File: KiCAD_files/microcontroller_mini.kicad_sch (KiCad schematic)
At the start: 35 parts, among them J1 Conn_02x20_Top_Bottom, J2 USB_C_Receptacle_USB2.0, J8 FTSH-107-01-F-DV-K, SW1 KMR241NGLFS, SW2 KMR241NGLFS, U1 STM32G474RE, U3 WE-TVS-82400102, U4 AP1117-33, Y1 ECS-240-10-33-AGM-TR - 24MHz

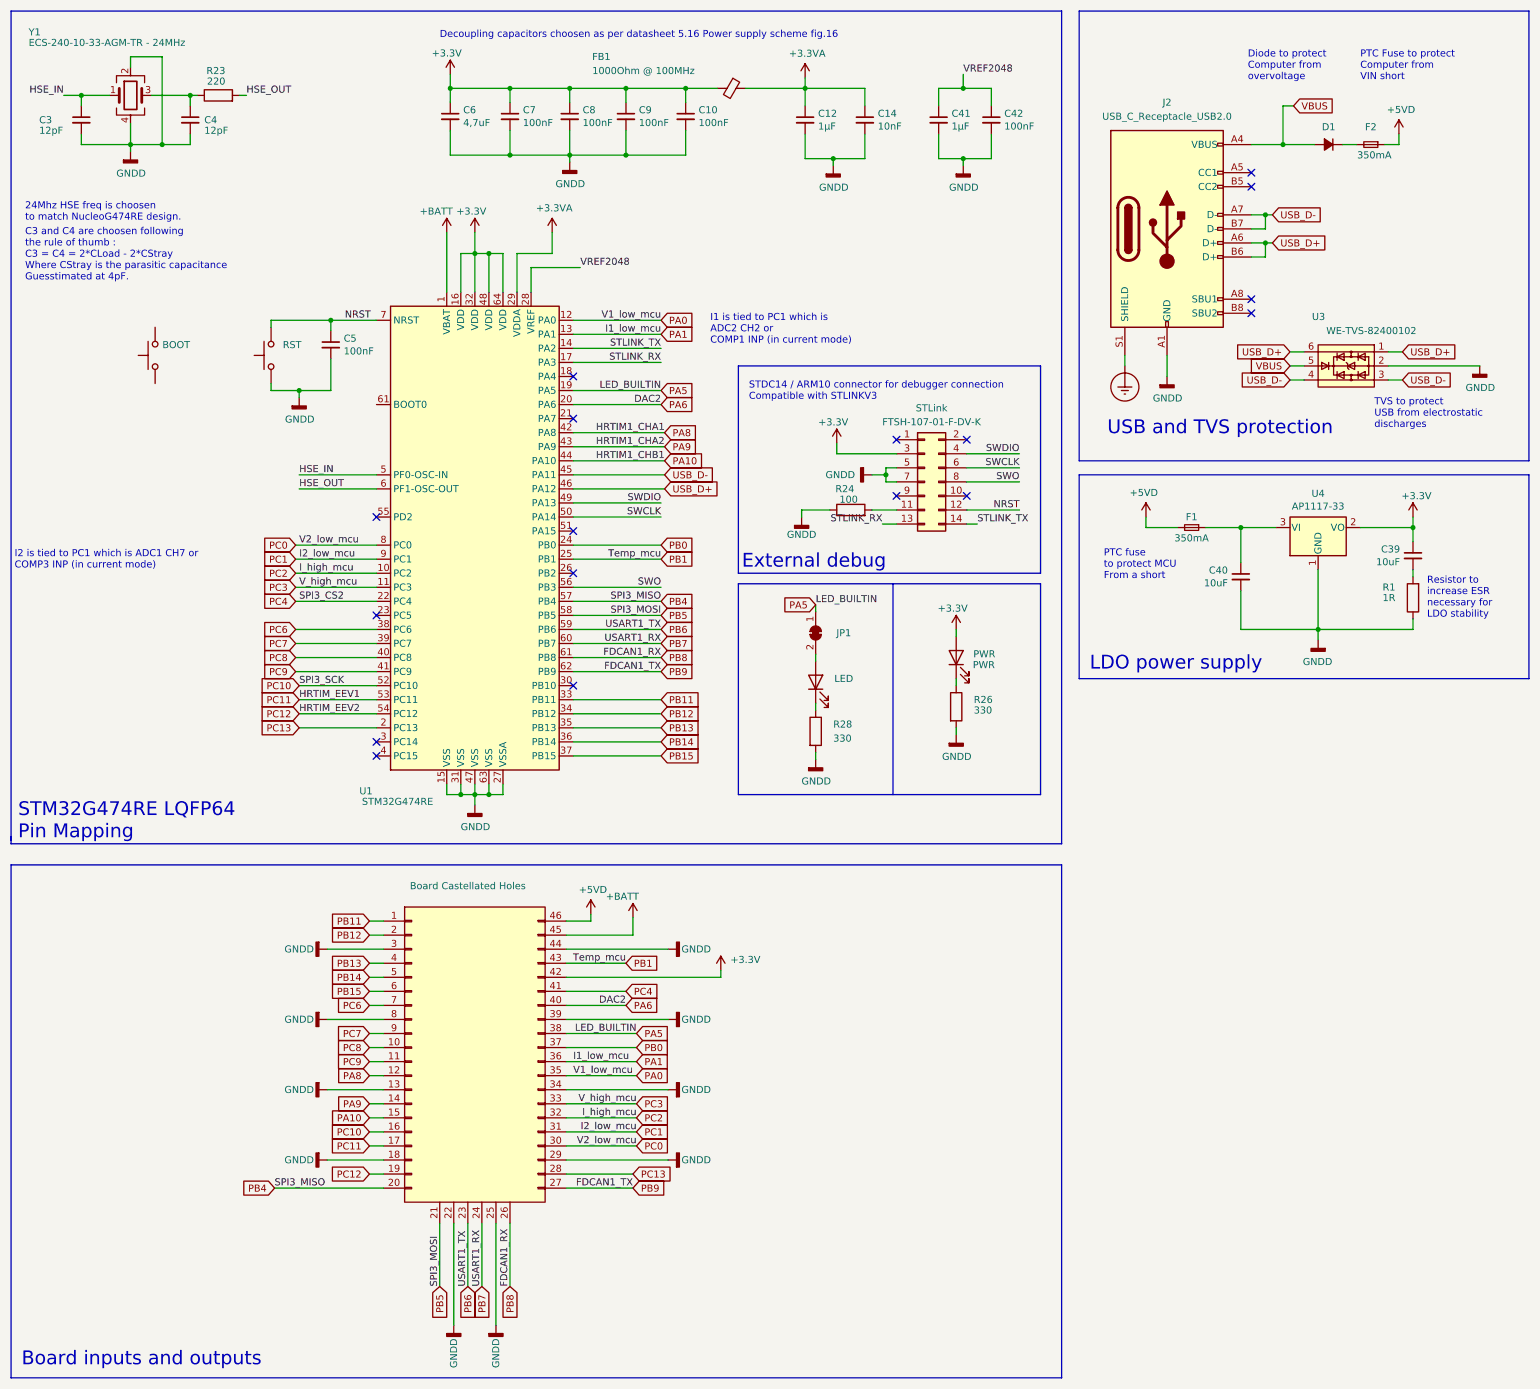
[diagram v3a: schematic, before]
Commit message: WIP : Finalized the rework of the MCU board. Added extra pins to be able to interact with all the native pinout of the G474 Choosen to deploy the bootloader pin on PC14, it will require a custom bootloader.
Former-commit-id: c1ded6b4e2272d08c1bdd5e172bcf8412ac79a26
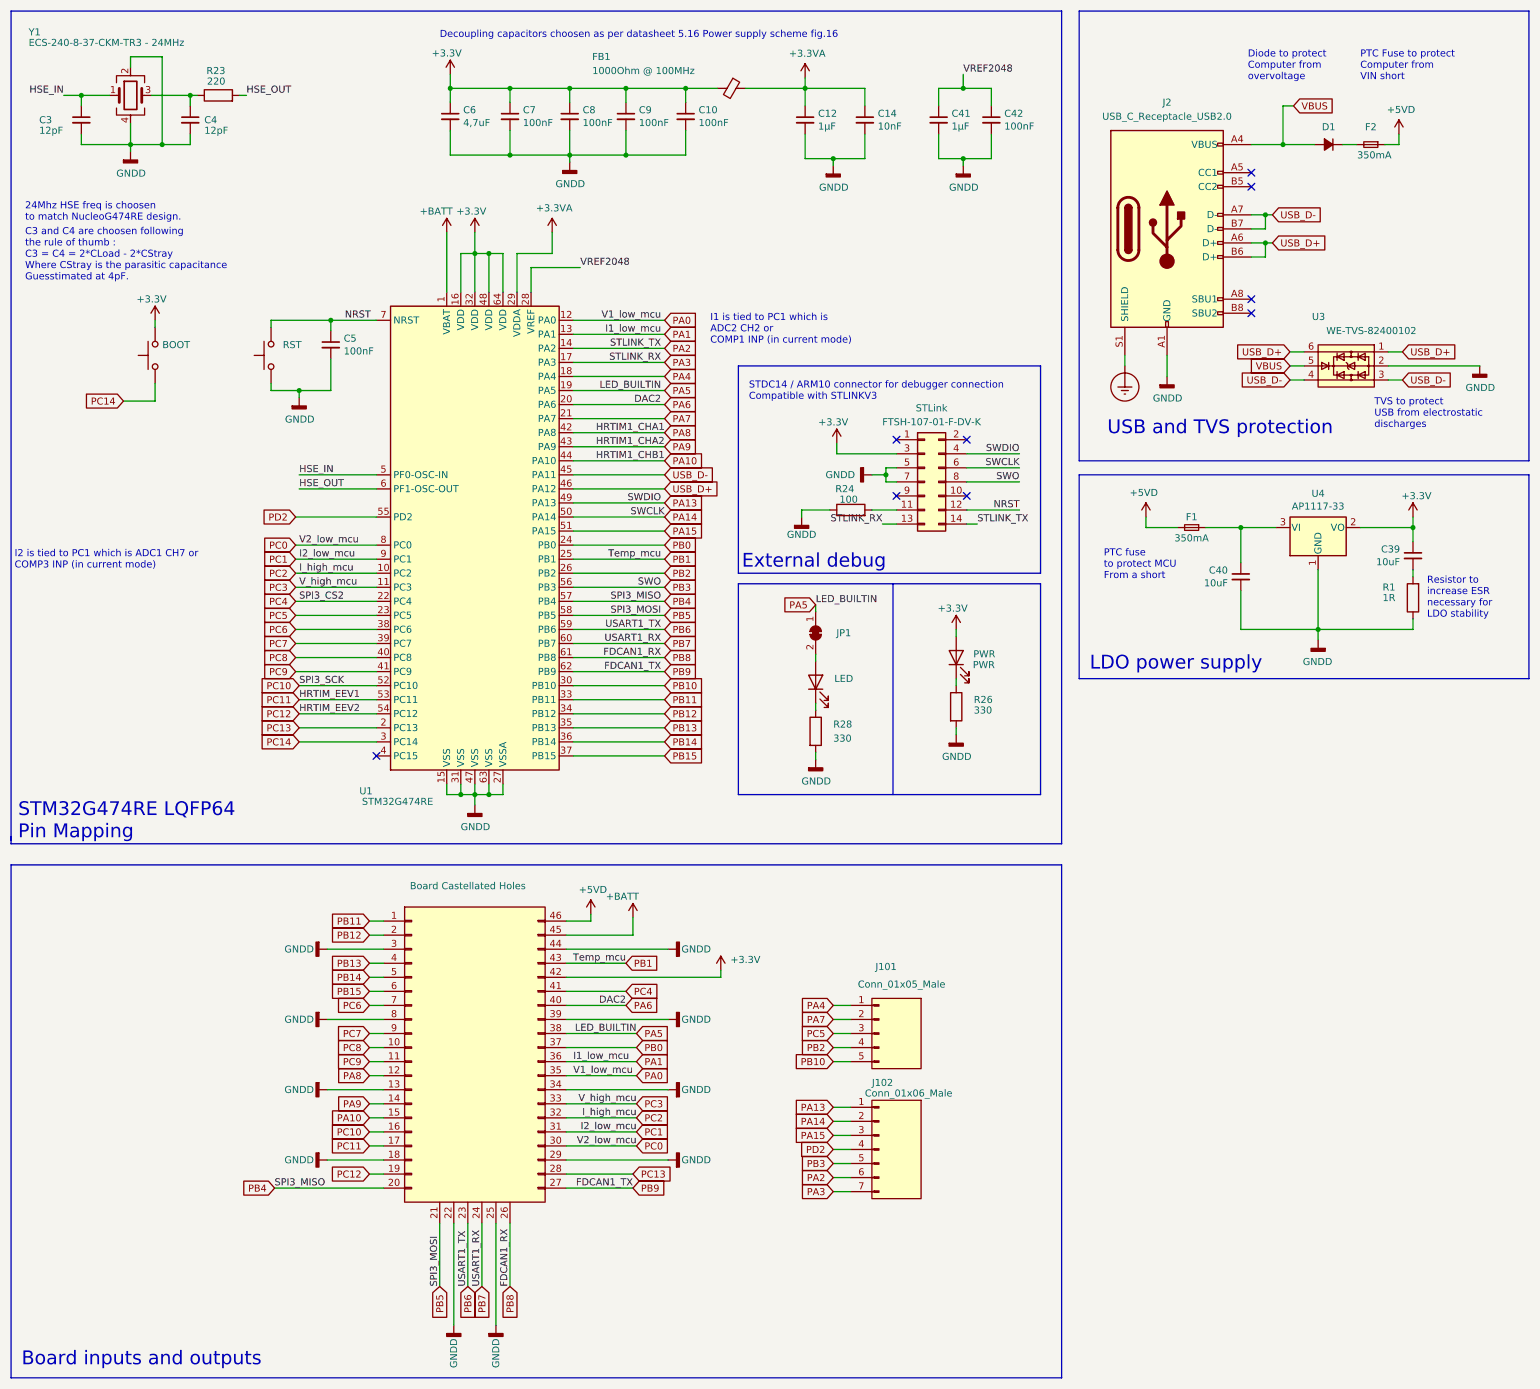
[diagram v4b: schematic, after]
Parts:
- added J101: Conn_01x05_Male, Footprints:PinHeader_1x05_P2.54mm_Vertical, symbol Connector:Conn_01x05_Male
- added J102: Conn_01x06_Male, Footprints:PinHeader_1x07_P2.54mm_Vertical, symbol Connector:Conn_01x07_Male
- Y1: value ECS-240-10-33-AGM-TR - 24MHz -> ECS-240-8-37-CKM-TR3 - 24MHz; footprint Crystal:Crystal_SMD_3225-4Pin_3.2x2.5mm -> Crystal:Crystal_SMD_2016-4Pin_2.0x1.6mm; Manf# ECS-240-10-33-AGM-TR -> ECS-240-8-37-CKM-TR3
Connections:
- net +3V3: now also SW2.2
- net PA4: now reaches U1.18 (PA4)
- net PA4: now also J101.1 (Pin_1)
- net PA7: now reaches U1.21 (PA7)
- net PA7: now also J101.2 (Pin_2)
- net PC5: now reaches U1.23 (PC5)
- net PC5: now also J101.3 (Pin_3)
- net PB2: now reaches U1.26 (PB2)
- net PB2: now also J101.4 (Pin_4)
- net PC14: now reaches U1.3 (PC14)
- net PC14: now also SW2.1
- net PB10: now reaches U1.30 (PB10)
- net PB10: now also J101.5 (Pin_5)
- net PA15: now reaches U1.51 (PA15)
- net PA15: now also J102.3 (Pin_3)
- net PD2: now reaches U1.55 (PD2)
- net PD2: now also J102.4 (Pin_4)
- net STLINK_RX renamed PA3
- net PA3: now also J102.7 (Pin_7)
- net STLINK_TX renamed PA2
- net PA2: now also J102.6 (Pin_6)
- net SWCLK renamed PA14
- net PA14: now also J102.2 (Pin_2)
- net SWDIO renamed PA13
- net PA13: now also J102.1 (Pin_1)
- net SWO renamed PB3
- net PB3: now also J102.5 (Pin_5)
- no-connect marks 17 -> 9

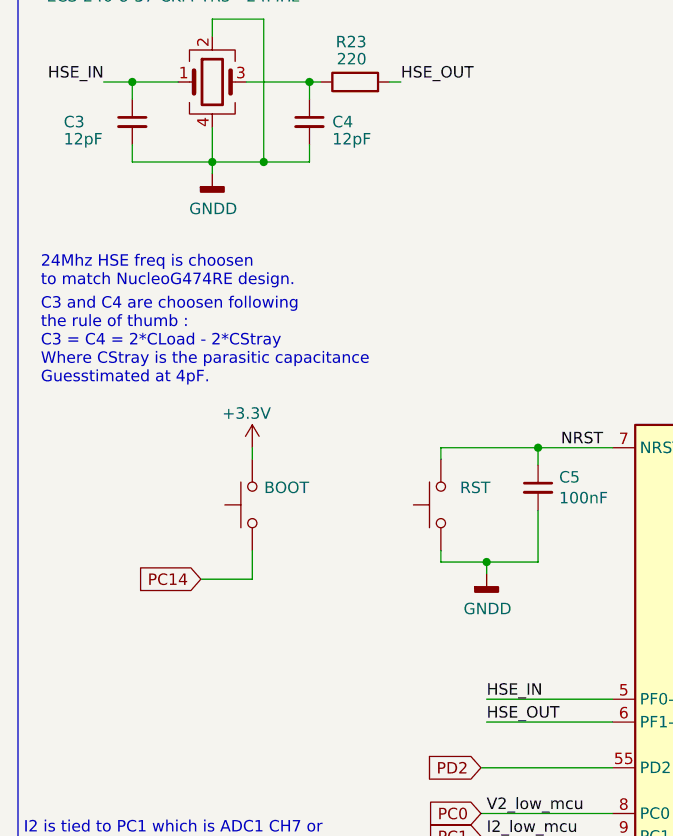
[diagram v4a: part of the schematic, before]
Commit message: WIP : Refined the crystal GND keepout, polished the bottom overlay
Former-commit-id: 2906c1a23d44a8ddcb814e6c8993671dfbd082db
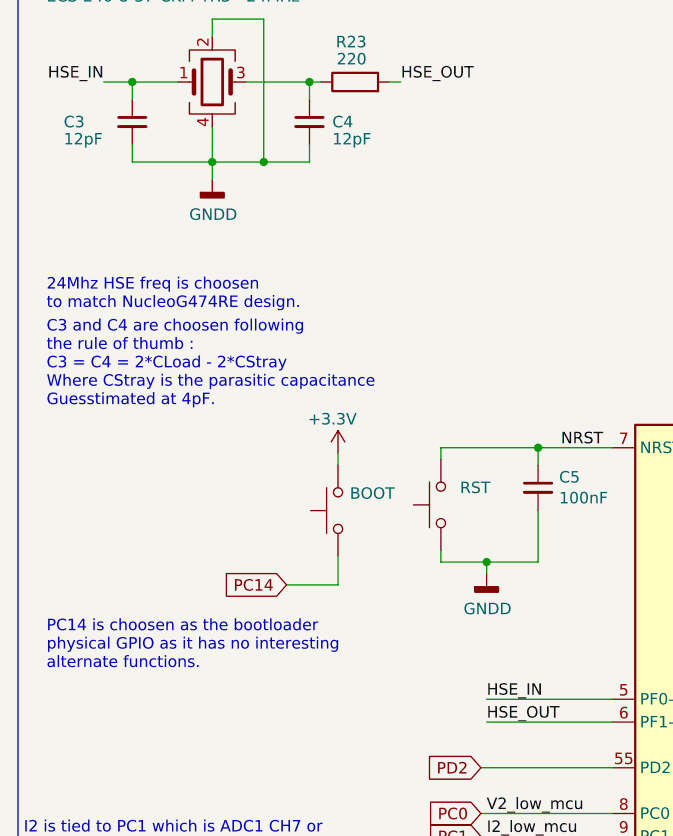
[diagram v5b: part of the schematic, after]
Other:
- note added: "PC14 is choosen as the bootloader physical GPIO as it has no interesting alternate functions."
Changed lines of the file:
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@@
   (no_connect (at 177.8 100.33))
   (no_connect (at 83.82 157.48))
-  (wire (pts (xy 43.815 78.74) (xy 43.815 80.01))
+  (wire (pts (xy 53.34 79.375) (xy 53.34 80.645))
     (stroke (width 0) (type default) (color 0 0 0 0))
   )
@@
     (stroke (width 0) (type default) (color 0 0 0 0))
   )
-  (wire (pts (xy 39.37 46.99) (xy 39.37 48.26))
-    (stroke (width 0) (type default) (color 0 0 0 0))
-  )
   (polyline (pts (xy 207.645 177.165) (xy 17.78 177.165))
     (stroke (width 0) (type default) (color 0 0 0 0))
@@
     (stroke (width 0) (type default) (color 0 0 0 0))
   )
-  (wire (pts (xy 43.815 90.17) (xy 43.815 93.345))
+  (wire (pts (xy 53.34 90.805) (xy 53.34 93.98))
     (stroke (width 0) (type default) (color 0 0 0 0))
   )
@@
     (stroke (width 0) (type default) (color 0 0 0 0))
   )
-  (wire (pts (xy 38.1 93.345) (xy 43.815 93.345))
+  (wire (pts (xy 47.625 93.98) (xy 53.34 93.98))
     (stroke (width 0) (type default) (color 0 0 0 0))
   )
@@
     (stroke (width 0) (type default) (color 0 0 0 0))
   )
+  (wire (pts (xy 39.37 46.99) (xy 39.37 48.895))
+    (stroke (width 0) (type default) (color 0 0 0 0))
+  )
   (wire (pts (xy 119.38 91.44) (xy 135.89 91.44))
     (stroke (width 0) (type default) (color 0 0 0 0))
@@
   (wire (pts (xy 172.085 40.005) (xy 172.085 36.83))
     (stroke (width 0) (type default) (color 0 0 0 0))
+  )
+  (text "PC14 is choosen as the bootloader \nphysical GPIO as it has no interesting\nalternate functions."
+    (at 20.955 103.505 0)
+    (effects (font (size 1.27 1.27)) (justify left bottom))
   )
   (text "PTC Fuse to protect \nComputer from \nVIN short" (at 261.62 35.56 0)
@@
   )
   (text "C3 and C4 are choosen following \nthe rule of thumb : \nC3 = C4 = 2*CLoad - 2*CStray \nWhere CStray is the parasitic capacitance\nGuesstimated at 4pF."
-    (at 20.32 71.755 0)
+    (at 20.955 74.295 0)
     (effects (font (size 1.27 1.27)) (justify left bottom))
   )
@@
   )
   (text "24Mhz HSE freq is choosen\nto match NucleoG474RE design. "
-    (at 20.32 60.96 0)
+    (at 20.955 63.5 0)
     (effects (font (size 1.27 1.27)) (justify left bottom))
   )
@@
     )
   )
-  (global_label "PC14" (shape input) (at 38.1 93.345 180) (fields_autoplaced)
-    (effects (font (size 1.27 1.27)) (justify right))
-    (property "Références Inter-Feuilles" "${INTERSHEET_REFS}" (id 0) (at 30.7279 93.2656 0)
+  (global_label "PC14" (shape input) (at 47.625 93.98 180) (fields_autoplaced)
+    (effects (font (size 1.27 1.27)) (justify right))
+    (property "Références Inter-Feuilles" "${INTERSHEET_REFS}" (id 0) (at 40.2529 93.9006 0)
       (effects (font (size 1.27 1.27)) (justify right) hide)
     )
@@
     (pin "2")
   )
-  (symbol (lib_id "power:GNDD") (at 39.37 48.26 0) (unit 1)
-    (in_bom yes) (on_board yes)
-    (property "Reference" "#PWR01" (id 0) (at 39.37 54.61 0)
-      (effects (font (size 1.27 1.27)) hide)
-    )
-    (property "Value" "GNDD" (id 1) (at 39.4716 52.197 0))
-    (property "Footprint" "" (id 2) (at 39.37 48.26 0)
-      (effects (font (size 1.27 1.27)) hide)
-    )
-    (property "Datasheet" "" (id 3) (at 39.37 48.26 0)
+  (symbol (lib_id "power:GNDD") (at 39.37 48.895 0) (unit 1)
+    (in_bom yes) (on_board yes)
+    (property "Reference" "#PWR01" (id 0) (at 39.37 55.245 0)
+      (effects (font (size 1.27 1.27)) hide)
+    )
+    (property "Value" "GNDD" (id 1) (at 39.4716 52.832 0))
+    (property "Footprint" "" (id 2) (at 39.37 48.895 0)
+      (effects (font (size 1.27 1.27)) hide)
+    )
+    (property "Datasheet" "" (id 3) (at 39.37 48.895 0)
       (effects (font (size 1.27 1.27)) hide)
     )
@@
     (pin "1")
   )
-  (symbol (lib_id "Switch:SW_Push") (at 43.815 85.09 90) (unit 1)
-    (in_bom yes) (on_board yes)
-    (property "Reference" "SW2" (id 0) (at 45.0342 83.9216 90)
-      (effects (font (size 1.27 1.27)) (justify right) hide)
-    )
-    (property "Value" "KMR241NGLFS" (id 1) (at 45.0342 86.233 90)
-      (effects (font (size 1.27 1.27)) (justify right) hide)
-    )
-    (property "Footprint" "Button_Switch_SMD:SW_Push_1P1T_NO_CK_KMR2" (id 2) (at 38.735 85.09 0)
-      (effects (font (size 1.27 1.27)) hide)
-    )
-    (property "Datasheet" "~" (id 3) (at 38.735 85.09 0)
-      (effects (font (size 1.27 1.27)) hide)
-    )
-    (property "Manf#" "KMR241NGLFS" (id 4) (at 43.815 85.09 0)
-      (effects (font (size 1.27 1.27)) hide)
-    )
-    (property "Name" "BOOT" (id 5) (at 47.625 83.185 90))
+  (symbol (lib_id "Switch:SW_Push") (at 53.34 85.725 90) (unit 1)
+    (in_bom yes) (on_board yes)
+    (property "Reference" "SW2" (id 0) (at 54.5592 84.5566 90)
+      (effects (font (size 1.27 1.27)) (justify right) hide)
+    )
+    (property "Value" "KMR241NGLFS" (id 1) (at 54.5592 86.868 90)
+      (effects (font (size 1.27 1.27)) (justify right) hide)
+    )
+    (property "Footprint" "Button_Switch_SMD:SW_Push_1P1T_NO_CK_KMR2" (id 2) (at 48.26 85.725 0)
+      (effects (font (size 1.27 1.27)) hide)
+    )
+    (property "Datasheet" "~" (id 3) (at 48.26 85.725 0)
+      (effects (font (size 1.27 1.27)) hide)
+    )
+    (property "Manf#" "KMR241NGLFS" (id 4) (at 53.34 85.725 0)
+      (effects (font (size 1.27 1.27)) hide)
+    )
+    (property "Name" "BOOT" (id 5) (at 57.15 83.82 90))
     (pin "1")
     (pin "2")
@@
     (pin "1")
   )
-  (symbol (lib_id "power:+3.3V") (at 43.815 78.74 0) (unit 1)
-    (in_bom yes) (on_board yes)
-    (property "Reference" "#PWR0109" (id 0) (at 43.815 82.55 0)
-      (effects (font (size 1.27 1.27)) hide)
-    )
-    (property "Value" "+3.3V" (id 1) (at 43.18 74.93 0))
-    (property "Footprint" "" (id 2) (at 43.815 78.74 0)
-      (effects (font (size 1.27 1.27)) hide)
-    )
-    (property "Datasheet" "" (id 3) (at 43.815 78.74 0)
-      (effects (font (size 1.27 1.27)) hide)
-    )
+  (symbol (lib_id "power:+3.3V") (at 53.34 79.375 0) (unit 1)
+    (in_bom yes) (on_board yes)
+    (property "Reference" "#PWR0109" (id 0) (at 53.34 83.185 0)
+      (effects (font (size 1.27 1.27)) hide)
+    )
+    (property "Value" "+3.3V" (id 1) (at 52.705 75.565 0))
+    (property "Footprint" "" (id 2) (at 53.34 79.375 0)
+      (effects (font (size 1.27 1.27)) hide)
+    )
+    (property "Datasheet" "" (id 3) (at 53.34 79.375 0)
+      (effects (font (size 1.27 1.27)) hide)
+    )

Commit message: Added necessary information for BOM ordering
Former-commit-id: 116c703b052ef693f4f6c94bbef521d6efde9abc
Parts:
- C10, C14, C3, C4, C42, C5, C7, C8, C9, FB1, R1, R23, R24, R26, R28: Footprint-BOM (none) -> 0402
- C12, C41, C6: Footprint-BOM (none) -> 0603
- C39, C40, LED1, LED2: Footprint-BOM (none) -> 0805
- D1: Footprint-BOM (none) -> SOD523; Manf# (none) -> 1N4448X-TP
- F1, F2: Footprint-BOM (none) -> 0805; Manf# (none) -> 0ZCK0035FF2G
- J1, J101, J102, JP1: DNP (none) -> x; Manf# (none) -> DNP
- J2: LCSC (none) -> C165948; Manf# (none) -> USB4105-GF-A-120
- U1: Footprint-BOM (none) -> LQFP-64
- U3: Footprint-BOM (none) -> SOT23-6; Manf# (none) -> 82400102
- U4: value AP1117-33 -> AZ1117-33; Footprint-BOM (none) -> SOT89-3; Manf# AP1117E33G-13 -> AZ1117CR-3.3TRG1
- Y1: Footprint-BOM (none) -> 2016
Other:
- moved on the sheet: FB1, R24
